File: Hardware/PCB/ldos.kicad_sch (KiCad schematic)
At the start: 9 parts, among them U10 AZ1117-5.0, U9 TLV75533PDRV

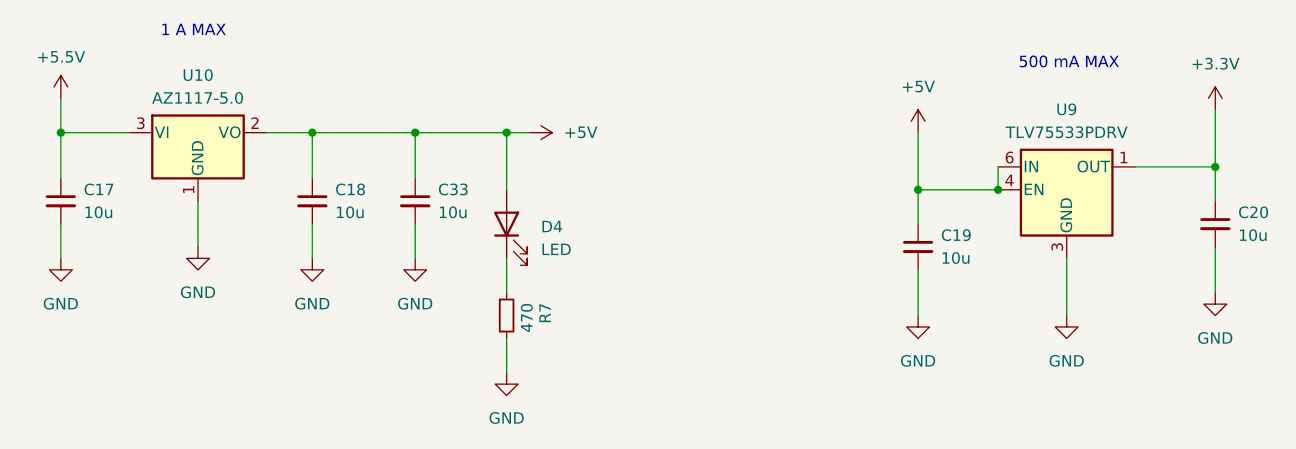
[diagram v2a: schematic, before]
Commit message: pcb layout and routing pretty much done, checking DRC
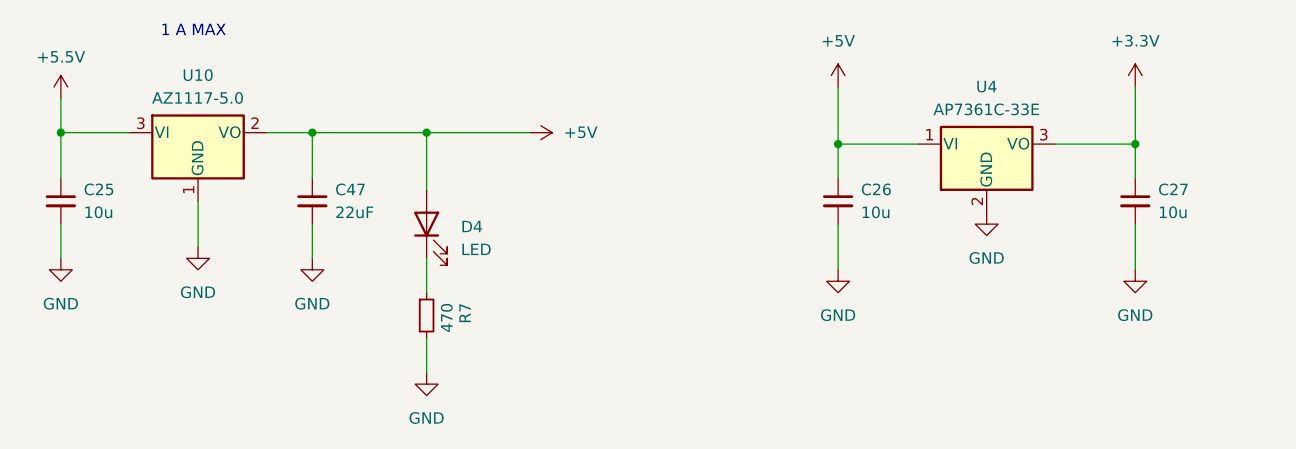
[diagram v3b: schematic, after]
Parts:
- removed C17: 10u, Capacitor_SMD:C_1206_3216Metric_Pad1.33x1.80mm_HandSolder, symbol Device:C_Small
- removed C18, C19, C20, C33: 10u, Capacitor_SMD:C_0805_2012Metric_Pad1.18x1.45mm_HandSolder, symbol Device:C_Small
- removed U9: TLV75533PDRV, Package_SON:WSON-6-1EP_2x2mm_P0.65mm_EP1x1.6mm, symbol Regulator_Linear:TLV75533PDRV
- added C25, C26, C27: 10u, Capacitor_SMD:C_0805_2012Metric_Pad1.18x1.45mm_HandSolder, symbol Device:C_Small
- added C47: 22uF, Capacitor_SMD:C_0805_2012Metric_Pad1.18x1.45mm_HandSolder, symbol Device:C_Small
- added U4: AP7361C-33E, Package_TO_SOT_SMD:SOT-223-3_TabPin2, symbol Regulator_Linear:AP7361C-33E
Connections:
- net +3.3V: now also C27.1, U4.3 (VO)
- net +5.5V: now also C25.1
- net +5V: now also C26.1, C47.1, U4.1 (VI)
- net GND: now also C25.2, C26.2, C27.2, C47.2, U4.2 (GND)
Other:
- note removed: "500 mA MAX"
- moved on the sheet: D4, R7

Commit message: fixed BOM, added some silkscreen, getting quote now
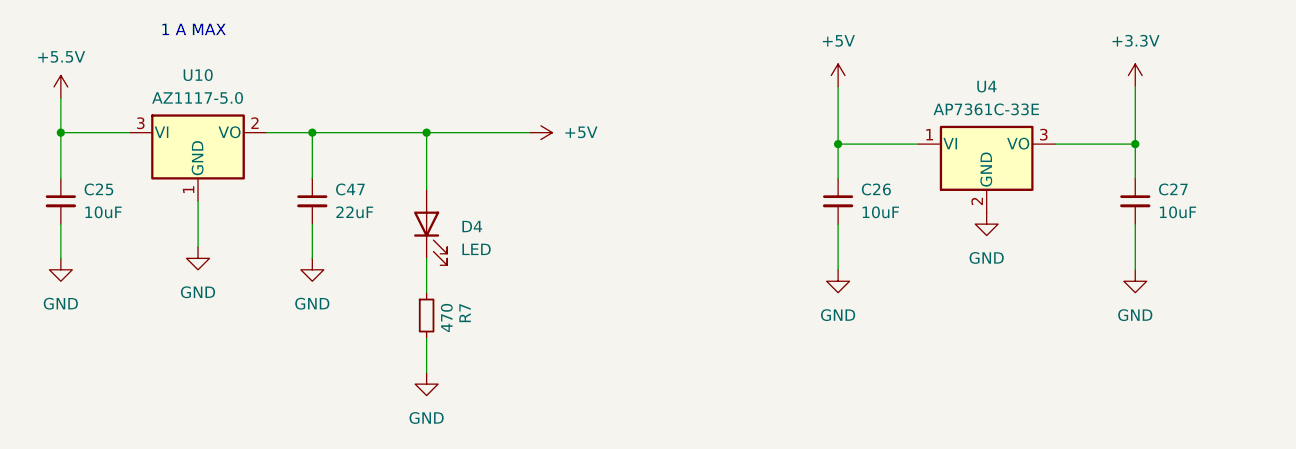
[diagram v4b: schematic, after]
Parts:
- C25, C26, C27: value 10u -> 10uF
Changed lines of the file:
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@@
 			)
 		)
-		(property "Value" "10u"
+		(property "Value" "10uF"
 			(at 44.45 57.1562 0)
 			(effects
@@
 			)
 		)
-		(property "Value" "10u"
+		(property "Value" "10uF"
 			(at 163.83 57.1562 0)
 			(effects
@@
 			)
 		)
-		(property "Value" "10u"
+		(property "Value" "10uF"
 			(at 130.81 57.1562 0)
 			(effects

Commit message: kinda pricey, I should try to make a smaller version using LCSC parts for cheaper solution
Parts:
- C25, C26, C27: LCSC (none) -> C307520
- C47: LCSC (none) -> C398815
- D4: LCSC (none) -> C125093
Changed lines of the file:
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@@
+			)
+		)
+		(property "LCSC" "C398815"
+			(at 69.85 55.88 0)
+			(effects
+				(font
+					(size 1.27 1.27)
+				)
 			)
 		)
@@
 			)
 		)
+		(property "LCSC" ""
+			(at 144.78 49.53 0)
+			(effects
+				(font
+					(size 1.27 1.27)
+				)
+			)
+		)
 		(pin "2"
 		)
@@
 			)
 		)
+		(property "LCSC" "C307520"
+			(at 41.91 55.88 0)
+			(effects
+				(font
+					(size 1.27 1.27)
+				)
+			)
+		)
 		(pin "2"
 		)
@@
 			)
 		)
+		(property "LCSC" "C307520"
+			(at 161.29 55.88 0)
+			(effects
+				(font
+					(size 1.27 1.27)
+				)
+			)
+		)
 		(pin "2"
 		)
@@
 			)
 		)
+		(property "LCSC" "C125093"
+			(at 82.55 58.42 0)
+			(effects
+				(font
+					(size 1.27 1.27)
+				)
+			)
+		)
 		(pin "1"
 		)
@@
 				)
 				(hide yes)
+			)
+		)
+		(property "LCSC" ""
+			(at 82.55 68.58 0)
+			(effects
+				(font
+					(size 1.27 1.27)
+				)
 			)
 		)
@@
 			)
 		)
+		(property "LCSC" ""
+			(at 57.15 48.26 0)
+			(effects
+				(font
+					(size 1.27 1.27)
+				)
+			)
+		)
 		(pin "1"
 		)
@@
 			)
 		)
+		(property "LCSC" "C307520"
+			(at 128.27 55.88 0)
+			(effects
+				(font
+					(size 1.27 1.27)
+				)
+			)
+		)

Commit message: done with this, placed order
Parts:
- removed C27: 10uF, Capacitor_SMD:C_0805_2012Metric_Pad1.18x1.45mm_HandSolder, symbol Device:C_Small
- removed D4: LED, LED_SMD:LED_0603_1608Metric_Pad1.05x0.95mm_HandSolder, symbol Device:LED
- removed R7: 470, Resistor_SMD:R_0603_1608Metric_Pad0.98x0.95mm_HandSolder, symbol Device:R_Small
- removed U4: AP7361C-33E, Package_TO_SOT_SMD:SOT-223-3_TabPin2, symbol Regulator_Linear:AP7361C-33E
- added C50: 22uF, Capacitor_SMD:C_0805_2012Metric_Pad1.18x1.45mm_HandSolder, symbol Device:C_Small
- added U12: AZ1117-3.3, Package_TO_SOT_SMD:SOT-223-3_TabPin2, symbol Regulator_Linear:AZ1117-3.3
- C25, C26: footprint Capacitor_SMD:C_0805_2012Metric_Pad1.18x1.45mm_HandSolder -> Capacitor_SMD:C_0603_1608Metric_Pad1.08x0.95mm_HandSolder; LCSC C307520 -> C96446; MPN CL21A106KOQNNNG -> CL10A106MA8NRNC
- C47: LCSC C398815 -> C602037; MPN CL21A226MOCLRNC -> CL21A226MAYNNNE
- U10: LCSC (none) -> C108496
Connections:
- net +3.3V: now also C50.1, U12.2 (VO)
- net +5V: now also U12.3 (VI)
- net GND: now also C50.2, U12.1 (GND)
